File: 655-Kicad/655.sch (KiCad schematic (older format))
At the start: 168 parts, among them IC1 ATMEGA32U4, J1 USBMINI_B05, P1 CONN_1, P2 CONN_1, P3 CONN_1, P4 CONN_1, P5 CONN_1, P6 CONN_1, SW0:0 F0, SW0:1 CTRL, SW0:10 CMD, SW0:11 ALT, SW0:12 CTRL, SW0:13 ←, SW0:14 ↓, SW0:15 →, SW0:2 ALT, SW0:3 CMD, SW0:7 SPACE, SW1:0 F1, SW1:1 SHIFT, SW1:10 ,, SW1:11 ., SW1:12 ?, SW1:13 SHIFT, SW1:14 ↑, SW1:15 END, SW1:3 Z, SW1:4 X, SW1:5 C, SW1:6 V, SW1:7 B, SW1:8 N, SW1:9 M, SW2:0 F2, SW2:1 CAPS, SW2:10 L, SW2:11 ;, SW2:12 ', SW2:14 ENTER, SW2:15 PGDWN, SW2:2 A, SW2:3 S, SW2:4 D, SW2:5 F, SW2:6 G, SW2:7 H, SW2:8 J, SW2:9 K, SW3:0 F3, SW3:1 TAB, SW3:10 O, SW3:11 P, SW3:12 {, SW3:13 }, SW3:14 BCKSL, SW3:15 PGUP, SW3:2 Q, SW3:3 W, SW3:4 E, SW3:5 R, SW3:6 T, SW3:7 Y, SW3:8 U, SW3:9 I, SW4:0 F4, SW4:1 TILDE, SW4:10 9, SW4:11 0, SW4:12 -, SW4:13 =, SW4:14 BCKSP, SW4:15 ESC, SW4:2 1, SW4:3 2, SW4:4 3, SW4:5 4, SW4:6 5, SW4:7 6, SW4:8 7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

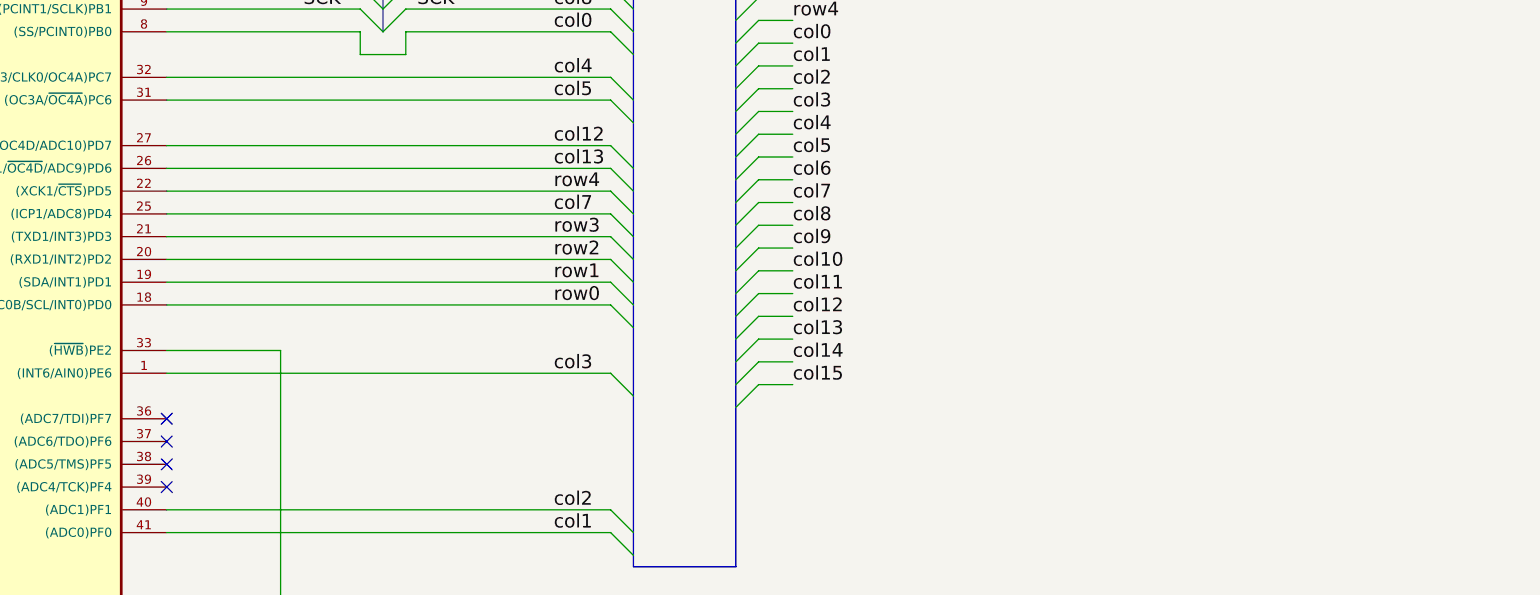
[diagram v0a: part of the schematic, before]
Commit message: change resistor footprints to 0805R, add caps led
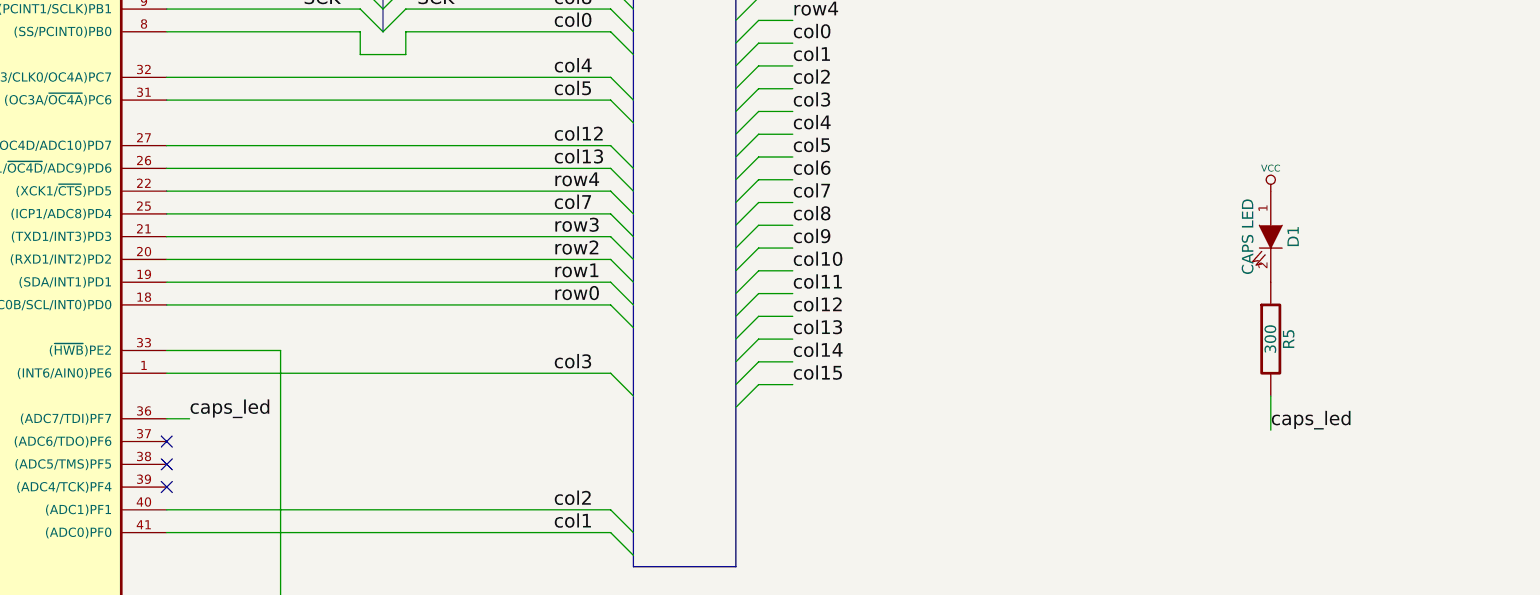
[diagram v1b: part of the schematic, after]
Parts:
- added D1: CAPS LED, mx1a:MX1A-led, symbol LED
- added R5: 300, 0805:0805R, symbol R
- R1, R2, R3, R4: footprint res:resistor -> 0805:0805R
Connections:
- net VCC: now also D1.1 (A)
- net caps_led: now reaches IC1.36 ((ADC7/TDI)PF7)
- net caps_led: now also R5.2
- new net: D1.2 (K), R5.1
- no-connect marks 8 -> 7

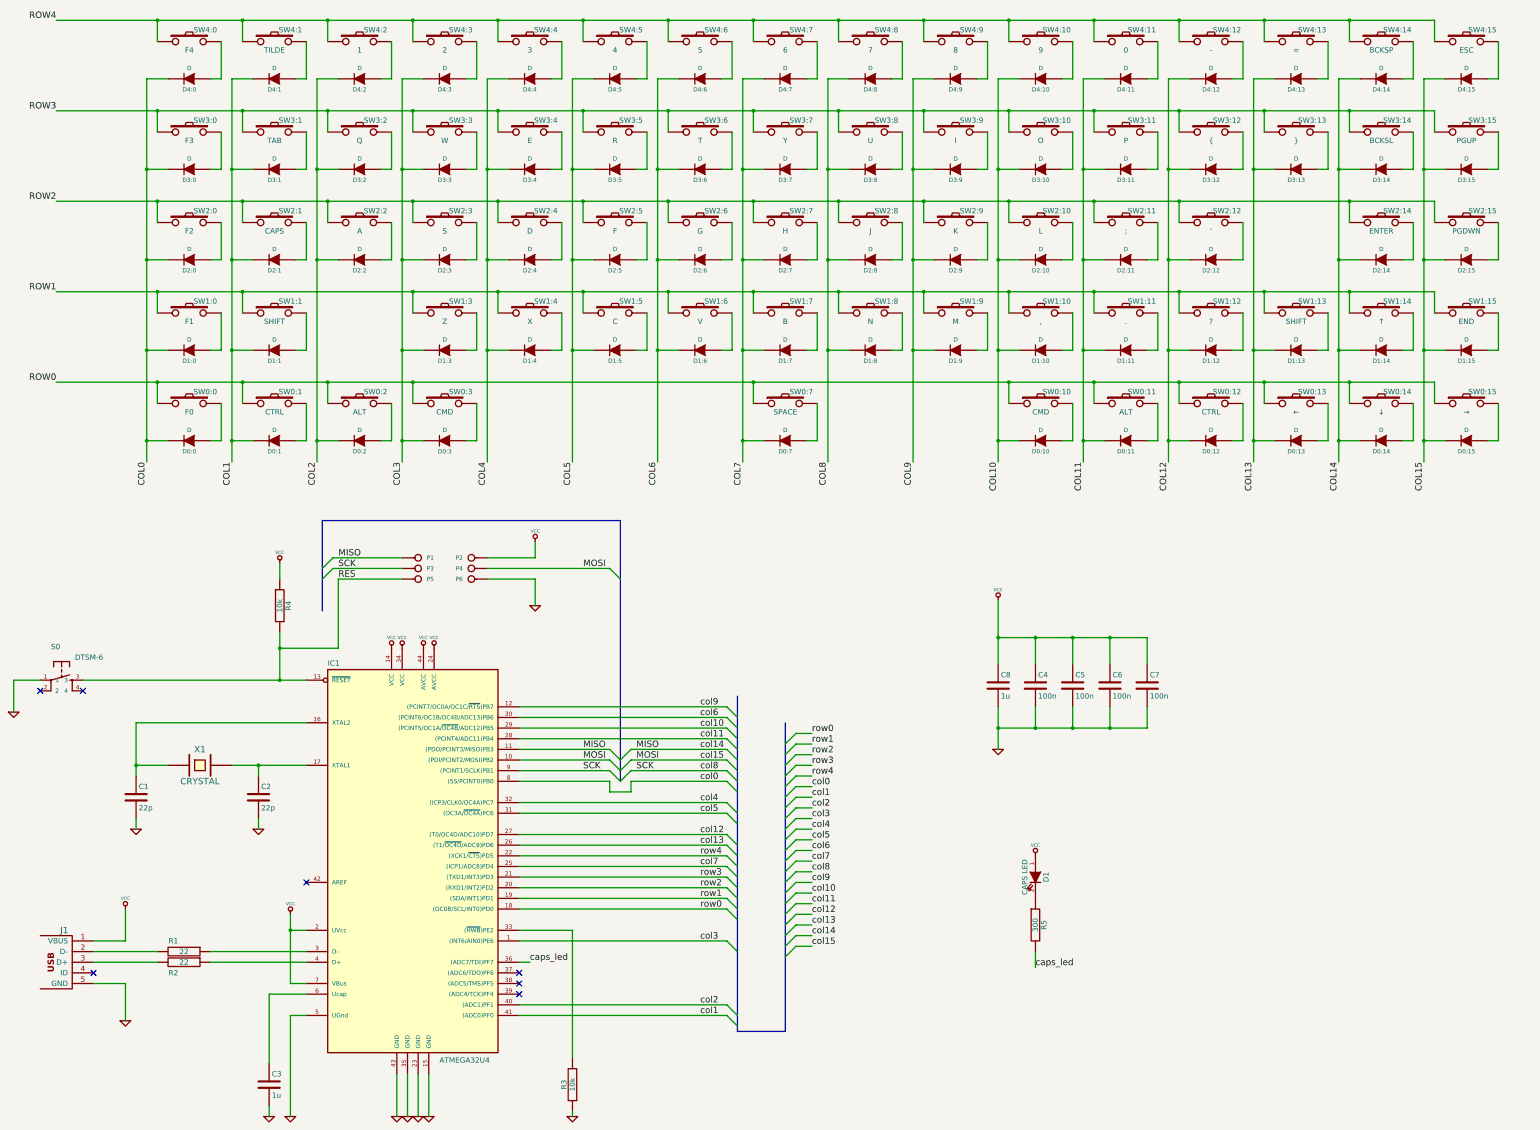
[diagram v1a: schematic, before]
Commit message: fixing up matrix, re zoning, no routes
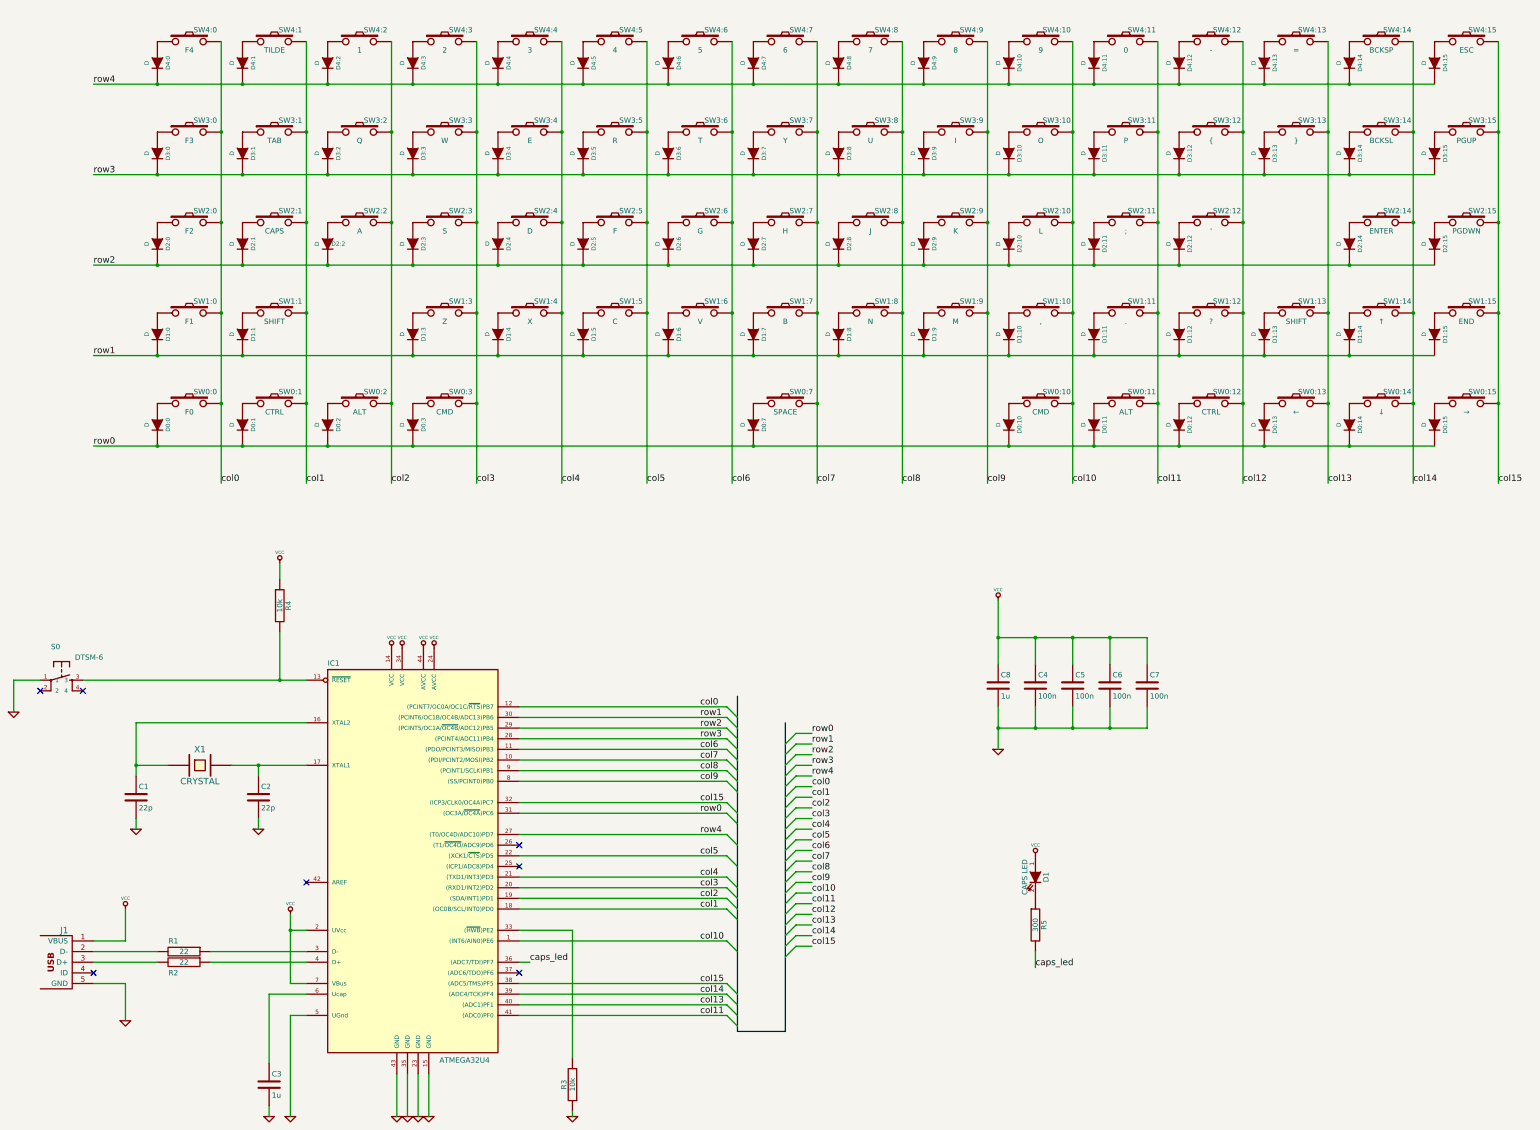
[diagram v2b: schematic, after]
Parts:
- removed P1, P2, P3, P4, P5, P6: CONN_1, pin:pad, symbol CONN_1
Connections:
- net MISO is gone; now on net col6: IC1.11 ((PDO/PCINT3/MISO)PB3)
- net MOSI is gone; now on net col7: IC1.10 ((PDI/PCINT2/MOSI)PB2)
- net col0: now also IC1.12 ((PCINT7/OC0A/OC1C/~RTS~)PB7), SW0:0.2, SW1:0.2, SW2:0.2, SW3:0.2, SW4:0.2; no longer IC1.8 ((SS/PCINT0)PB0)
- net col1: now also IC1.18 ((OC0B/SCL/INT0)PD0), SW0:1.2, SW1:1.2, SW2:1.2, SW3:1.2, SW4:1.2; no longer IC1.41 ((ADC0)PF0)
- net col10: now also IC1.1 ((INT6/AIN0)PE6), SW0:10.2, SW1:10.2, SW2:10.2, SW3:10.2, SW4:10.2; no longer IC1.29 ((PCINT5/OC1A/~OC4B~/ADC12)PB5)
- net col11: now also IC1.41 ((ADC0)PF0), SW0:11.2, SW1:11.2, SW2:11.2, SW3:11.2, SW4:11.2; no longer IC1.28 ((PCINT4/ADC11)PB4)
- net col12: now also SW0:12.2, SW1:12.2, SW2:12.2, SW3:12.2, SW4:12.2; no longer IC1.27 ((T0/OC4D/ADC10)PD7)
- net col13: now also IC1.40 ((ADC1)PF1), SW0:13.2, SW1:13.2, SW3:13.2, SW4:13.2; no longer IC1.26 ((T1/~OC4D~/ADC9)PD6)
- net col2: now also IC1.19 ((SDA/INT1)PD1), SW0:2.2, SW2:2.2, SW3:2.2, SW4:2.2; no longer IC1.40 ((ADC1)PF1)
- net col3: now also IC1.20 ((RXD1/INT2)PD2), SW0:3.2, SW1:3.2, SW2:3.2, SW3:3.2, SW4:3.2; no longer IC1.1 ((INT6/AIN0)PE6)
- net col4: now also IC1.21 ((TXD1/INT3)PD3), SW1:4.2, SW2:4.2, SW3:4.2, SW4:4.2; no longer IC1.32 ((ICP3/CLK0/OC4A)PC7)
- net col5: now also IC1.22 ((XCK1/~CTS~)PD5), SW1:5.2, SW2:5.2, SW3:5.2, SW4:5.2; no longer IC1.31 ((OC3A/~OC4A~)PC6)
- net col6: now also SW1:6.2, SW2:6.2, SW3:6.2, SW4:6.2; no longer IC1.30 ((PCINT6/OC1B/OC4B/ADC13)PB6)
- net col7: now also SW0:7.2, SW1:7.2, SW2:7.2, SW3:7.2, SW4:7.2; no longer IC1.25 ((ICP1/ADC8)PD4)
- net col9: now also IC1.8 ((SS/PCINT0)PB0), SW1:9.2, SW2:9.2, SW3:9.2, SW4:9.2; no longer IC1.12 ((PCINT7/OC0A/OC1C/~RTS~)PB7)
- net row0: now also D0:0.2 (K), D0:1.2 (K), D0:10.2 (K), D0:11.2 (K), D0:12.2 (K), D0:13.2 (K), D0:14.2 (K), D0:15.2 (K), D0:2.2 (K), D0:3.2 (K), D0:7.2 (K), IC1.31 ((OC3A/~OC4A~)PC6); no longer IC1.18 ((OC0B/SCL/INT0)PD0)
- net row1: now also D1:0.2 (K), D1:1.2 (K), D1:10.2 (K), D1:11.2 (K), D1:12.2 (K), D1:13.2 (K), D1:14.2 (K), D1:15.2 (K), D1:3.2 (K), D1:4.2 (K), D1:5.2 (K), D1:6.2 (K), D1:7.2 (K), D1:8.2 (K), D1:9.2 (K), IC1.30 ((PCINT6/OC1B/OC4B/ADC13)PB6); no longer IC1.19 ((SDA/INT1)PD1)
- net row2: now also D2:0.2 (K), D2:1.2 (K), D2:10.2 (K), D2:11.2 (K), D2:12.2 (K), D2:14.2 (K), D2:15.2 (K), D2:2.2 (K), D2:3.2 (K), D2:4.2 (K), D2:5.2 (K), D2:6.2 (K), D2:7.2 (K), D2:8.2 (K), D2:9.2 (K), IC1.29 ((PCINT5/OC1A/~OC4B~/ADC12)PB5); no longer IC1.20 ((RXD1/INT2)PD2)
- net row3: now also D3:0.2 (K), D3:1.2 (K), D3:10.2 (K), D3:11.2 (K), D3:12.2 (K), D3:13.2 (K), D3:14.2 (K), D3:15.2 (K), D3:2.2 (K), D3:3.2 (K), D3:4.2 (K), D3:5.2 (K), D3:6.2 (K), D3:7.2 (K), D3:8.2 (K), D3:9.2 (K), IC1.28 ((PCINT4/ADC11)PB4); no longer IC1.21 ((TXD1/INT3)PD3)
- net row4: now also D4:0.2 (K), D4:1.2 (K), D4:10.2 (K), D4:11.2 (K), D4:12.2 (K), D4:13.2 (K), D4:14.2 (K), D4:15.2 (K), D4:2.2 (K), D4:3.2 (K), D4:4.2 (K), D4:5.2 (K), D4:6.2 (K), D4:7.2 (K), D4:8.2 (K), D4:9.2 (K), IC1.27 ((T0/OC4D/ADC10)PD7); no longer IC1.22 ((XCK1/~CTS~)PD5)
- net at D1:12.1 (A): now also SW1:12.1; no longer SW1:12.2
- net at D4:1.1 (A): now also SW4:1.1; no longer SW4:1.2
- net at D4:2.1 (A): now also SW4:2.1; no longer SW4:2.2
- net at D4:3.1 (A): now also SW4:3.1; no longer SW4:3.2
- net at D4:7.1 (A): now also SW4:7.1; no longer SW4:7.2
- net at D4:6.1 (A): now also SW4:6.1; no longer SW4:6.2
- net at D4:5.1 (A): now also SW4:5.1; no longer SW4:5.2
- net at D4:4.1 (A): now also SW4:4.1; no longer SW4:4.2
- net at D4:8.1 (A): now also SW4:8.1; no longer SW4:8.2
- net at D4:9.1 (A): now also SW4:9.1; no longer SW4:9.2
- net at D4:10.1 (A): now also SW4:10.1; no longer SW4:10.2
- net at D4:11.1 (A): now also SW4:11.1; no longer SW4:11.2
- net at D4:12.1 (A): now also SW4:12.1; no longer SW4:12.2
- net at D3:6.1 (A): now also SW3:6.1; no longer SW3:6.2
- net at D3:12.1 (A): now also SW3:12.1; no longer SW3:12.2
- net at D3:5.1 (A): now also SW3:5.1; no longer SW3:5.2
- net at D3:4.1 (A): now also SW3:4.1; no longer SW3:4.2
- net at D3:3.1 (A): now also SW3:3.1; no longer SW3:3.2
- net at D3:2.1 (A): now also SW3:2.1; no longer SW3:2.2
- net at D3:1.1 (A): now also SW3:1.1; no longer SW3:1.2
- net at D1:1.1 (A): now also SW1:1.1; no longer SW1:1.2
- net at D1:3.1 (A): now also SW1:3.1; no longer SW1:3.2
- net at D1:4.1 (A): now also SW1:4.1; no longer SW1:4.2
- net at D1:5.1 (A): now also SW1:5.1; no longer SW1:5.2
- net at D3:14.1 (A): now also SW3:14.1; no longer SW3:14.2
- net at D1:6.1 (A): now also SW1:6.1; no longer SW1:6.2
- net at D2:6.1 (A): now also SW2:6.1; no longer SW2:6.2
- net at D2:5.1 (A): now also SW2:5.1; no longer SW2:5.2
- net at D2:4.1 (A): now also SW2:4.1; no longer SW2:4.2
- net at D2:3.1 (A): now also SW2:3.1; no longer SW2:3.2
- net at D2:2.1 (A): now also SW2:2.1; no longer SW2:2.2
- net at D2:1.1 (A): now also SW2:1.1; no longer SW2:1.2
- net at D4:13.1 (A): now also SW4:13.1; no longer SW4:13.2
- net at D3:11.1 (A): now also SW3:11.1; no longer SW3:11.2
- net at D3:10.1 (A): now also SW3:10.1; no longer SW3:10.2
- net at D3:9.1 (A): now also SW3:9.1; no longer SW3:9.2
- net at D3:8.1 (A): now also SW3:8.1; no longer SW3:8.2
- net at D3:13.1 (A): now also SW3:13.1; no longer SW3:13.2
- net at D3:7.1 (A): now also SW3:7.1; no longer SW3:7.2
- net at D1:8.1 (A): now also SW1:8.1; no longer SW1:8.2
- net at D1:7.1 (A): now also SW1:7.1; no longer SW1:7.2
- net at D1:9.1 (A): now also SW1:9.1; no longer SW1:9.2
- net at D1:10.1 (A): now also SW1:10.1; no longer SW1:10.2
- net at D1:11.1 (A): now also SW1:11.1; no longer SW1:11.2
- net at D1:14.1 (A): now also SW1:14.1; no longer SW1:14.2
- net at D2:14.1 (A): now also SW2:14.1; no longer SW2:14.2
- net at D2:11.1 (A): now also SW2:11.1; no longer SW2:11.2
- net at D2:10.1 (A): now also SW2:10.1; no longer SW2:10.2
- net at D2:9.1 (A): now also SW2:9.1; no longer SW2:9.2
- net at D2:8.1 (A): now also SW2:8.1; no longer SW2:8.2
- net at D2:12.1 (A): now also SW2:12.1; no longer SW2:12.2
- net at D2:7.1 (A): now also SW2:7.1; no longer SW2:7.2
- net at D0:7.1 (A): now also SW0:7.1; no longer SW0:7.2
- net at D4:14.1 (A): now also SW4:14.1; no longer SW4:14.2
- net at D0:1.1 (A): now also SW0:1.1; no longer SW0:1.2
- net at D0:12.1 (A): now also SW0:12.1; no longer SW0:12.2
- net at D0:2.1 (A): now also SW0:2.1; no longer SW0:2.2
- net at D0:3.1 (A): now also SW0:3.1; no longer SW0:3.2
- net at D0:10.1 (A): now also SW0:10.1; no longer SW0:10.2
- net at D0:11.1 (A): now also SW0:11.1; no longer SW0:11.2
- net at D0:14.1 (A): now also SW0:14.1; no longer SW0:14.2
- net col15: now reaches IC1.38 ((ADC5/TMS)PF5)
- net col15: now also IC1.32 ((ICP3/CLK0/OC4A)PC7), SW0:15.2, SW1:15.2, SW2:15.2, SW3:15.2, SW4:15.2
- net col14: now reaches IC1.39 ((ADC4/TCK)PF4)
- net col14: now also SW0:14.2, SW1:14.2, SW2:14.2, SW3:14.2, SW4:14.2
- net at D4:0.1 (A): now also SW4:0.1; no longer SW4:0.2
- net at D3:0.1 (A): now also SW3:0.1; no longer SW3:0.2
- net at D2:0.1 (A): now also SW2:0.1; no longer SW2:0.2
- net at D1:0.1 (A): now also SW1:0.1; no longer SW1:0.2
- net at D0:0.1 (A): now also SW0:0.1; no longer SW0:0.2
- net at D0:13.1 (A): now also SW0:13.1; no longer SW0:13.2
- net at D1:13.1 (A): now also SW1:13.1; no longer SW1:13.2
- net at D0:15.1 (A): now also SW0:15.1; no longer SW0:15.2
- net at D4:15.1 (A): now also SW4:15.1; no longer SW4:15.2
- net at D2:15.1 (A): now also SW2:15.1; no longer SW2:15.2
- net at D1:15.1 (A): now also SW1:15.1; no longer SW1:15.2
- net at D3:15.1 (A): now also SW3:15.1; no longer SW3:15.2
- removed net COL0: D0:0.2 (K), D1:0.2 (K), D2:0.2 (K), D3:0.2 (K), D4:0.2 (K)
- removed net COL1: D0:1.2 (K), D1:1.2 (K), D2:1.2 (K), D3:1.2 (K), D4:1.2 (K)
- removed net COL10: D0:10.2 (K), D1:10.2 (K), D2:10.2 (K), D3:10.2 (K), D4:10.2 (K)
- removed net COL11: D0:11.2 (K), D1:11.2 (K), D2:11.2 (K), D3:11.2 (K), D4:11.2 (K)
- removed net COL12: D0:12.2 (K), D1:12.2 (K), D2:12.2 (K), D3:12.2 (K), D4:12.2 (K)
- removed net COL13: D0:13.2 (K), D1:13.2 (K), D3:13.2 (K), D4:13.2 (K)
- removed net COL14: D0:14.2 (K), D1:14.2 (K), D2:14.2 (K), D3:14.2 (K), D4:14.2 (K)
- removed net COL15: D0:15.2 (K), D1:15.2 (K), D2:15.2 (K), D3:15.2 (K), D4:15.2 (K)
- removed net COL2: D0:2.2 (K), D2:2.2 (K), D3:2.2 (K), D4:2.2 (K)
- removed net COL3: D0:3.2 (K), D1:3.2 (K), D2:3.2 (K), D3:3.2 (K), D4:3.2 (K)
- removed net COL4: D1:4.2 (K), D2:4.2 (K), D3:4.2 (K), D4:4.2 (K)
- removed net COL5: D1:5.2 (K), D2:5.2 (K), D3:5.2 (K), D4:5.2 (K)
- removed net COL6: D1:6.2 (K), D2:6.2 (K), D3:6.2 (K), D4:6.2 (K)
- removed net COL7: D0:7.2 (K), D1:7.2 (K), D2:7.2 (K), D3:7.2 (K), D4:7.2 (K)
- removed net COL8: D1:8.2 (K), D2:8.2 (K), D3:8.2 (K), D4:8.2 (K)
- removed net COL9: D1:9.2 (K), D2:9.2 (K), D3:9.2 (K), D4:9.2 (K)
- net RES: no longer names the net of IC1.13 (~RESET~), R4.2, S0.3
- removed net ROW0: SW0:0.1, SW0:1.1, SW0:10.1, SW0:11.1, SW0:12.1, SW0:13.1, SW0:14.1, SW0:15.1, SW0:2.1, SW0:3.1, SW0:7.1
- removed net ROW1: SW1:0.1, SW1:1.1, SW1:10.1, SW1:11.1, SW1:12.1, SW1:13.1, SW1:14.1, SW1:15.1, SW1:3.1, SW1:4.1, SW1:5.1, SW1:6.1, SW1:7.1, SW1:8.1, SW1:9.1
- removed net ROW2: SW2:0.1, SW2:1.1, SW2:10.1, SW2:11.1, SW2:12.1, SW2:14.1, SW2:15.1, SW2:2.1, SW2:3.1, SW2:4.1, SW2:5.1, SW2:6.1, SW2:7.1, SW2:8.1, SW2:9.1
- removed net ROW3: SW3:0.1, SW3:1.1, SW3:10.1, SW3:11.1, SW3:12.1, SW3:13.1, SW3:14.1, SW3:15.1, SW3:2.1, SW3:3.1, SW3:4.1, SW3:5.1, SW3:6.1, SW3:7.1, SW3:8.1, SW3:9.1
- removed net ROW4: SW4:0.1, SW4:1.1, SW4:10.1, SW4:11.1, SW4:12.1, SW4:13.1, SW4:14.1, SW4:15.1, SW4:2.1, SW4:3.1, SW4:4.1, SW4:5.1, SW4:6.1, SW4:7.1, SW4:8.1, SW4:9.1
- net SCK renamed col8
- net col8: now also SW1:8.2, SW2:8.2, SW3:8.2, SW4:8.2
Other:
- moved on the sheet: D0:0, D0:1, D0:10, D0:11, D0:12, D0:13, D0:14, D0:15, D0:2, D0:3, D0:7, D1:0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
